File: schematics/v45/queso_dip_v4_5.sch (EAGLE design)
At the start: 49 parts, among them Q1 FOXSDLF/120-20, U1 PRTR5V0U2X,215, U2 PRTR5V0U2X,215, U3 PRTR5V0U2X,215, U4 PRTR5V0U2X,215, U5 PRTR5V0U2X,215, X1 USB-A-HU, X2 USB-A-HU, X3 USB-A-HU, X4 USB-A-HU

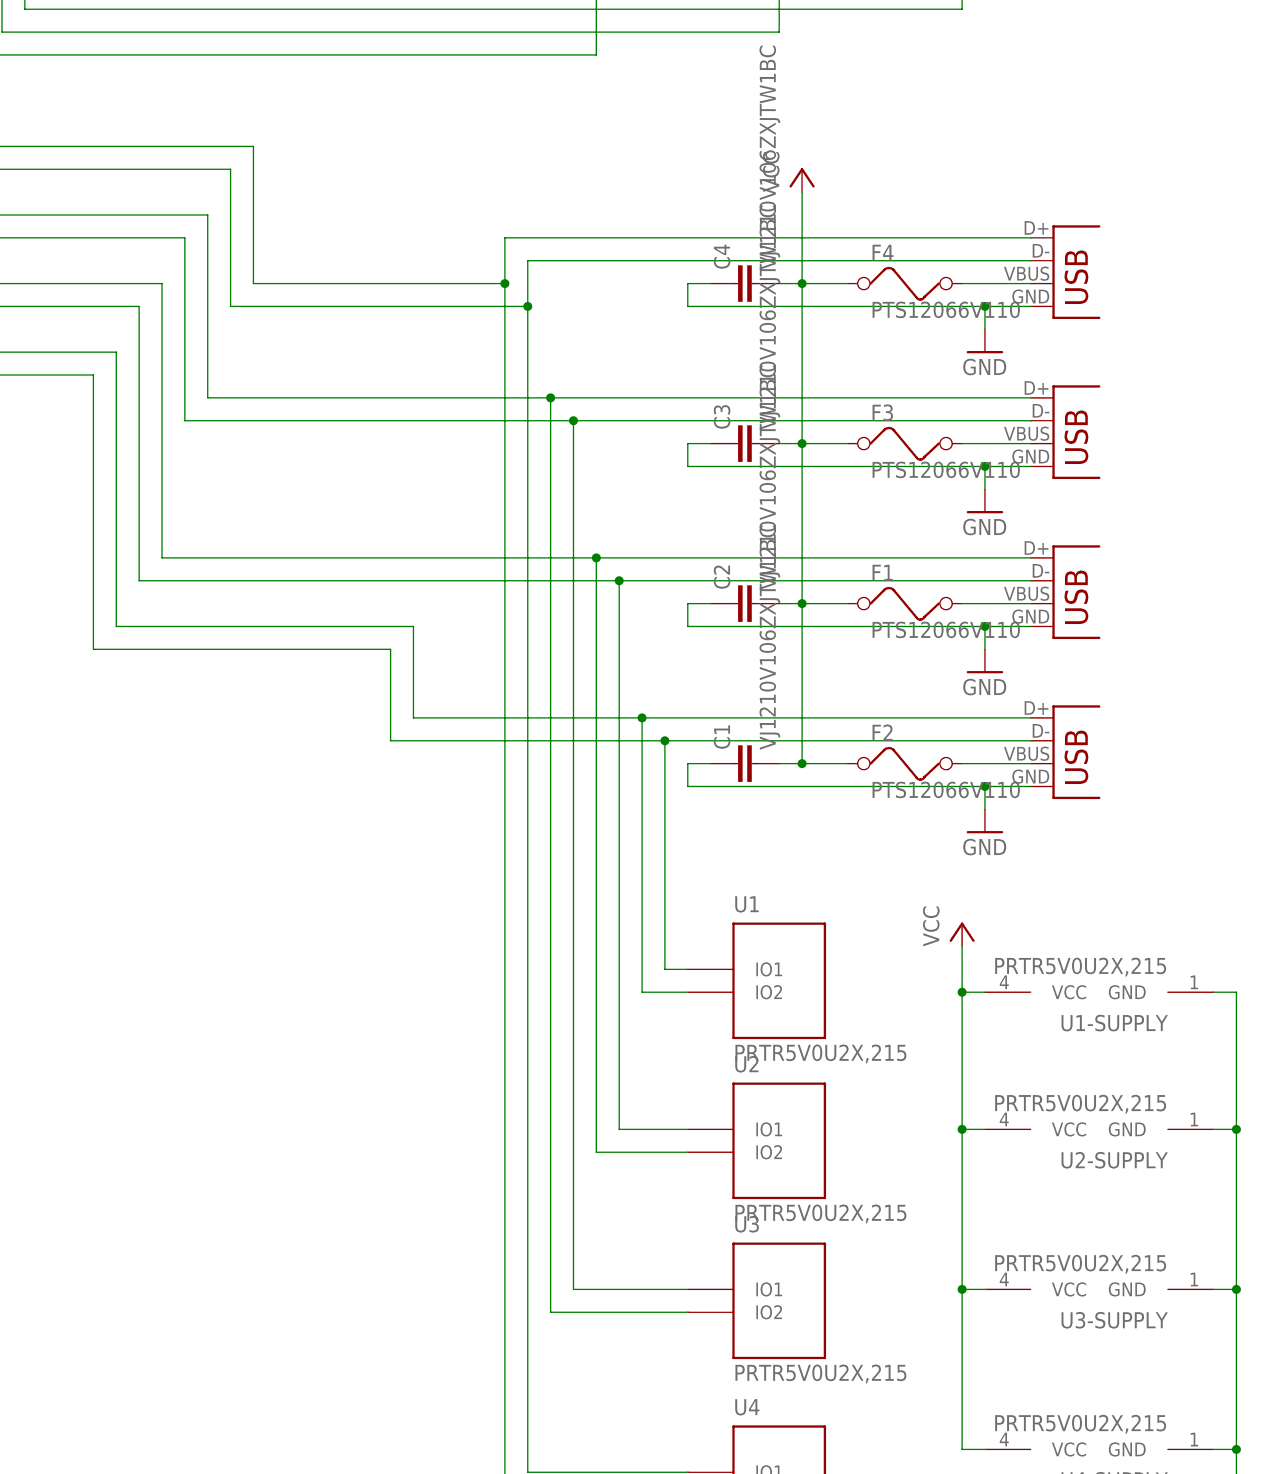
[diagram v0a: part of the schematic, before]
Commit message: sch + adapter
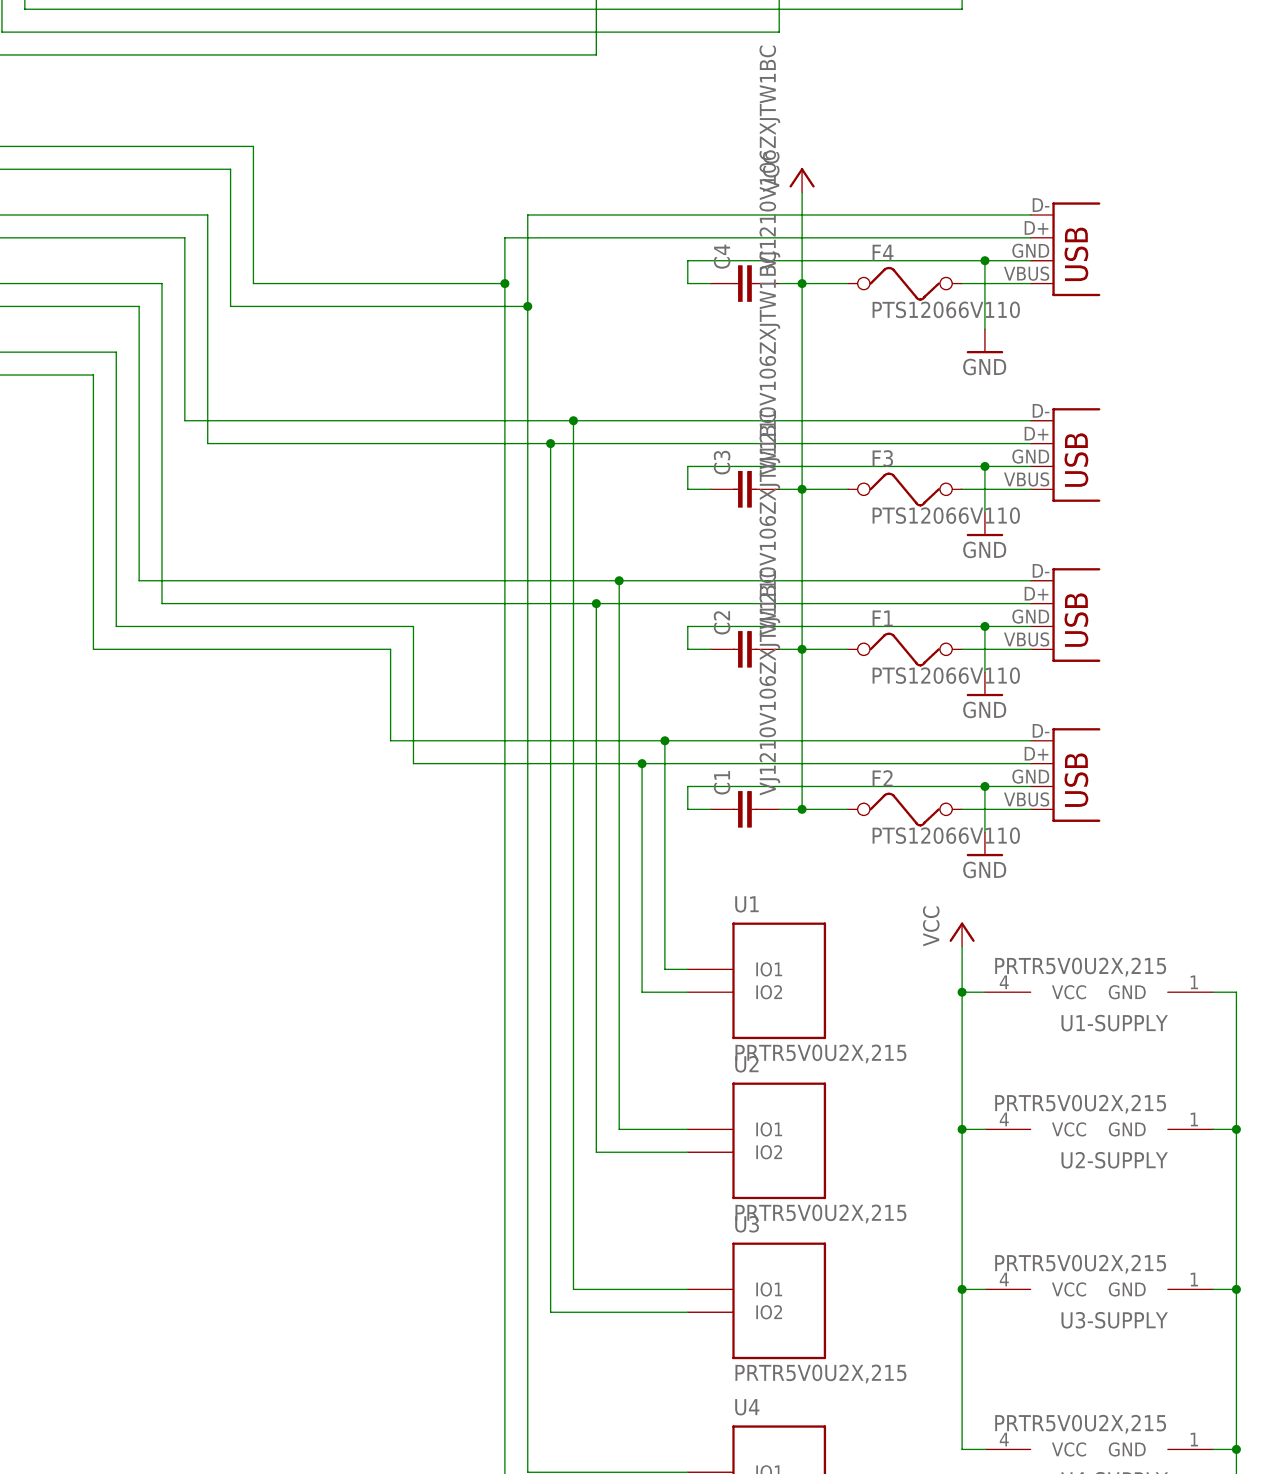
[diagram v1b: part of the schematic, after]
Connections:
- removed net N$10: F1.2, X2.VBUS
- removed net N$11: F3.2, X3.VBUS
- removed net N$12: F4.2, X4.VBUS
- new net N$3: F4.2, X4.GND
- new net N$4: F1.2, X2.GND
- new net N$5: F3.2, X3.GND
- net DM1: now also X4.D+; no longer X4.D-
- net DM2: now also X3.D+; no longer X3.D-
- net DM3: now also X2.D+; no longer X2.D-
- net DM4: now also X1.D+; no longer X1.D-
- net DP1: now also X4.D-; no longer X4.D+
- net DP2: now also X3.D-; no longer X3.D+
- net DP3: now also X2.D-; no longer X2.D+
- net DP4: now also X1.D-; no longer X1.D+
- net GND: now also X1.VBUS, X2.VBUS, X3.VBUS, X4.VBUS; no longer X1.GND, X2.GND, X3.GND, X4.GND
- net N$1: now also X1.GND; no longer X1.VBUS
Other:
- moved on the sheet: C1, C2, C3, F1, F2, F3
